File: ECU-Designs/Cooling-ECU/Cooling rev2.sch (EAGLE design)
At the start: 17 parts, among them T1 N-CHANNEL_MOSFETGENERIC, T2 N-CHANNEL_MOSFETGENERIC, T3 N-CHANNEL_MOSFETGENERIC, X1 MINIFIT_5566-12

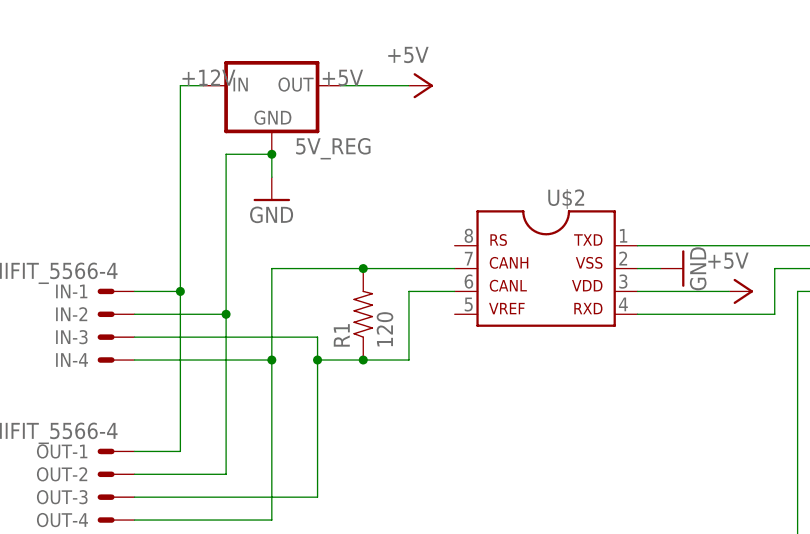
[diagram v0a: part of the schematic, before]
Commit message: Tried milling out cooling board
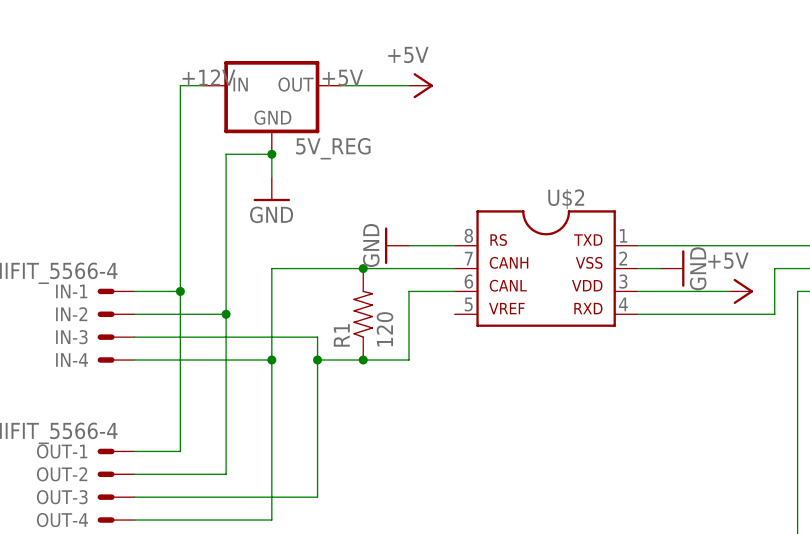
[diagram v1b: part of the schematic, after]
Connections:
- net GND: now also U$2.8
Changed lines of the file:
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@@
 <part name="G2" library="HyTechDevices" deviceset="GATE_DRIVE" device="ZXGD3003E6TA"/>
 <part name="G3" library="HyTechDevices" deviceset="GATE_DRIVE" device="ZXGD3003E6TA"/>
+<part name="GND13" library="supply1" deviceset="GND" device=""/>
 </parts>
 <sheets>
@@
 <instance part="G2" gate="G$1" x="152.4" y="20.32"/>
 <instance part="G3" gate="G$1" x="152.4" y="-5.08"/>
+<instance part="GND13" gate="1" x="-12.7" y="53.34" rot="R270"/>
 </instances>
 <busses>
@@
 <wire x1="243.84" y1="50.8" x2="228.6" y2="50.8" width="0.1524" layer="91"/>
 </segment>
+<segment>
+<pinref part="GND13" gate="1" pin="GND"/>
+<pinref part="U$2" gate="G$1" pin="8"/>
+<wire x1="-10.16" y1="53.34" x2="-5.08" y2="53.34" width="0.1524" layer="91"/>
+</segment>
 </net>

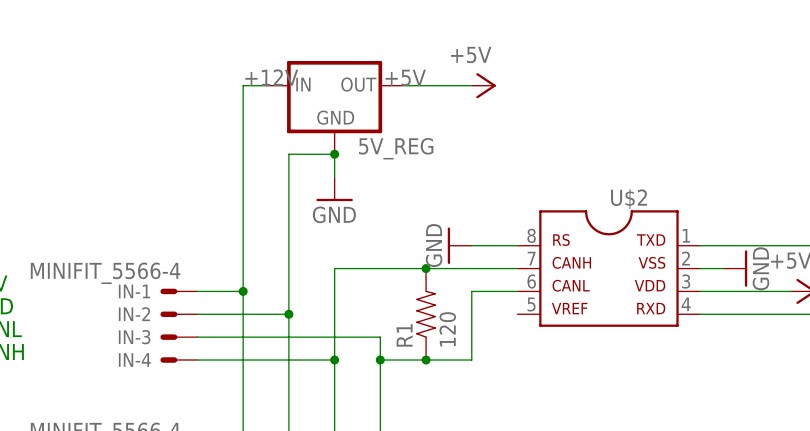
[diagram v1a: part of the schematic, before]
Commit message: Nathan screwed up the package so we had to blow stuff up
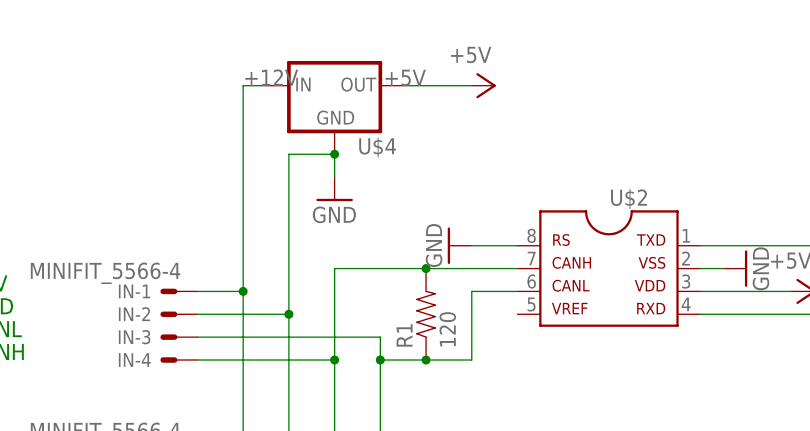
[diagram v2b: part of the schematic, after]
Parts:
- removed 5V_REG: (no value), HyTechDevices:5V_REGULATOR_LM340-NLM340MPX-5.0/NOPB
- added U$4: (no value), HyTechDevices:5VREG_LM340-NLM340MPX-5.0/NOPB
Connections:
- net +12V: now also U$4.IN; no longer 5V_REG.IN
- net +5V: now also U$4.OUT; no longer 5V_REG.OUT
- net GND: now also U$4.GND; no longer 5V_REG.GND
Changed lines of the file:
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@@
 </classes>
 <parts>
-<part name="5V_REG" library="HyTechDevices" deviceset="5V_REGULATOR_LM340-N" device="LM340MPX-5.0/NOPB"/>
 <part name="GND1" library="supply1" deviceset="GND" device=""/>
 <part name="U$2" library="HyTechDevices" deviceset="MCP2551" device=""/>
@@
 <part name="G3" library="HyTechDevices" deviceset="GATE_DRIVE" device="ZXGD3003E6TA"/>
 <part name="GND13" library="supply1" deviceset="GND" device=""/>
+<part name="U$4" library="HyTechDevices" deviceset="5VREG_LM340-N" device="LM340MPX-5.0/NOPB"/>
 </parts>
 <sheets>
@@
 </plain>
 <instances>
-<instance part="5V_REG" gate="G$1" x="-25.4" y="71.12"/>
 <instance part="GND1" gate="1" x="-25.4" y="58.42"/>
 <instance part="U$2" gate="G$1" x="12.7" y="45.72" rot="MR0"/>
@@
 <instance part="G3" gate="G$1" x="152.4" y="-5.08"/>
 <instance part="GND13" gate="1" x="-12.7" y="53.34" rot="R270"/>
+<instance part="U$4" gate="G$1" x="-25.4" y="71.12"/>
 </instances>
 <busses>
@@
 <net name="GND" class="0">
 <segment>
-<pinref part="5V_REG" gate="G$1" pin="GND"/>
 <pinref part="GND1" gate="1" pin="GND"/>
 <wire x1="-25.4" y1="63.5" x2="-25.4" y2="60.96" width="0.1524" layer="91"/>
-<junction x="-25.4" y="63.5"/>
 <pinref part="IN" gate="-2" pin="S"/>
 <wire x1="-40.64" y1="45.72" x2="-30.48" y2="45.72" width="0.1524" layer="91"/>
@@
 <pinref part="OUT" gate="-2" pin="S"/>
 <wire x1="-30.48" y1="27.94" x2="-40.64" y2="27.94" width="0.1524" layer="91"/>
+<pinref part="U$4" gate="G$1" pin="GND"/>
+<junction x="-25.4" y="63.5"/>
 </segment>
 <segment>
@@
 <net name="+5V" class="0">
 <segment>
-<pinref part="5V_REG" gate="G$1" pin="OUT"/>
 <wire x1="-10.16" y1="71.12" x2="-17.78" y2="71.12" width="0.1524" layer="91"/>
 <label x="-15.24" y="71.12" size="1.778" layer="95" rot="MR0"/>
 <pinref part="P+1" gate="1" pin="+5V"/>
+<pinref part="U$4" gate="G$1" pin="OUT"/>
 </segment>
 <segment>
@@
 </segment>
 <segment>
-<pinref part="5V_REG" gate="G$1" pin="IN"/>
 <wire x1="-33.02" y1="71.12" x2="-35.56" y2="71.12" width="0.1524" layer="91"/>
 <label x="-35.56" y="71.12" size="1.778" layer="95"/>
@@
 <pinref part="OUT" gate="-1" pin="S"/>
 <wire x1="-35.56" y1="30.48" x2="-40.64" y2="30.48" width="0.1524" layer="91"/>
-</segment>
-</net>
+<pinref part="U$4" gate="G$1" pin="IN"/>
+</segment>
+</net>
